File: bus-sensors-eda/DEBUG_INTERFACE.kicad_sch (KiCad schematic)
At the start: 8 parts, among them J2 Generic_Conn_01x05

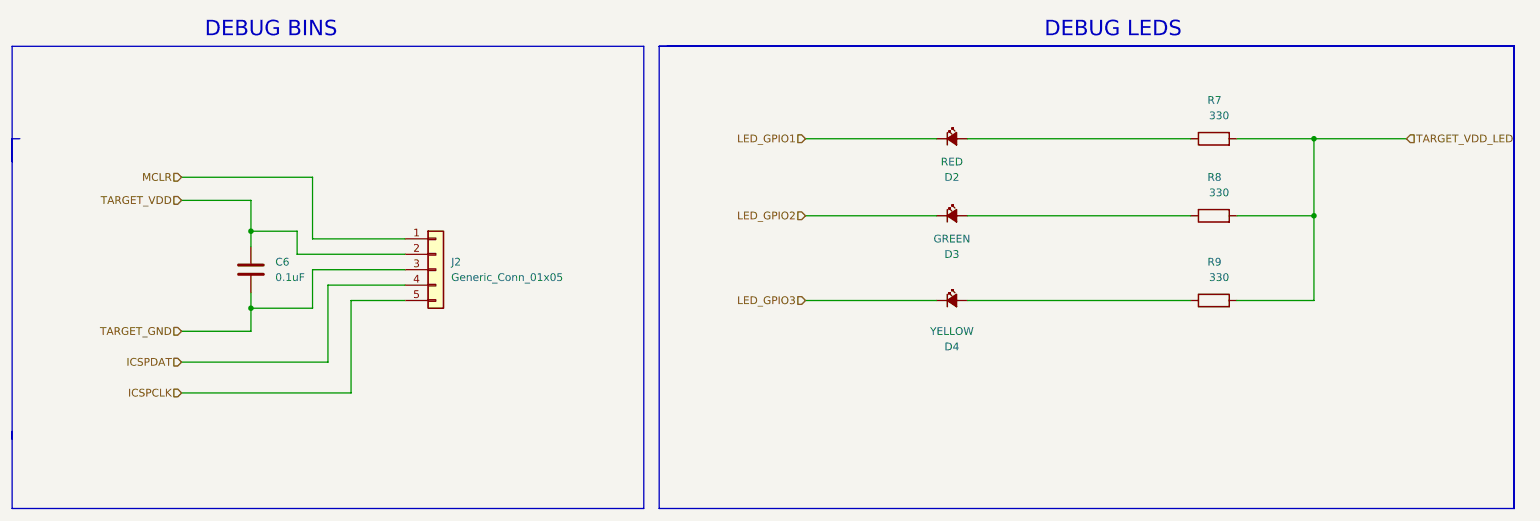
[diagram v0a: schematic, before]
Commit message: moving files under eda dir
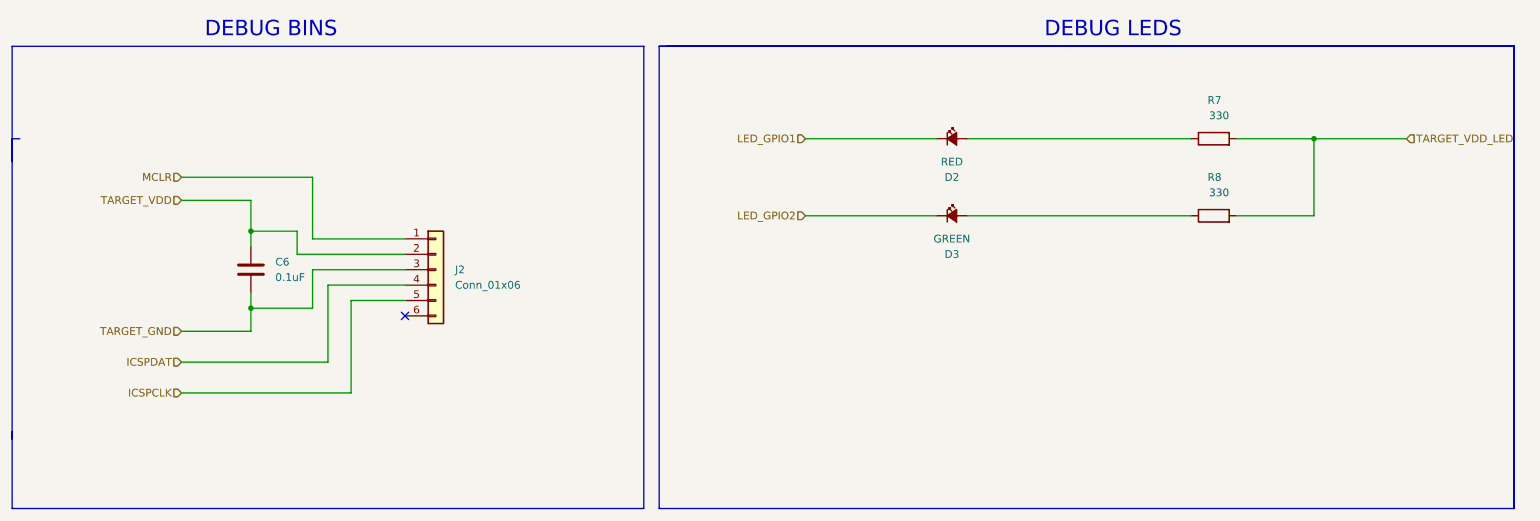
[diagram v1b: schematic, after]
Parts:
- removed D4: YELLOW, LED_SMD:LED_2512_6332Metric_Pad1.52x3.35mm_HandSolder, symbol Device:LED_Small_Filled
- removed J2: Generic_Conn_01x05, Connector_PinHeader_2.54mm:PinHeader_1x05_P2.54mm_Vertical, symbol avionics_board-cache:Connector_Generic_Conn_01x05
- removed R9: 330, Resistor_SMD:R_1210_3225Metric_Pad1.30x2.65mm_HandSolder, symbol Device:R
- added J2: Conn_01x06, Connector_PinHeader_2.54mm:PinHeader_1x06_P2.54mm_Horizontal, symbol Connector_Generic:Conn_01x06
- C6: footprint Capacitor_SMD:C_1812_4532Metric_Pad1.57x3.40mm_HandSolder -> Capacitor_SMD:C_1210_3225Metric_Pad1.33x2.70mm_HandSolder
- D2, D3: footprint LED_SMD:LED_2512_6332Metric_Pad1.52x3.35mm_HandSolder -> LED_SMD:LED_2010_5025Metric_Pad1.52x2.65mm_HandSolder
- R7, R8: footprint Resistor_SMD:R_1210_3225Metric_Pad1.30x2.65mm_HandSolder -> Resistor_SMD:R_2010_5025Metric_Pad1.40x2.65mm_HandSolder
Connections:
- net ICSPCLK: now also J2.5 (Pin_5)
- net ICSPDAT: now also J2.4 (Pin_4)
- net MCLR: now also J2.1 (Pin_1)
- net TARGET_GND: now also J2.3 (Pin_3)
- net TARGET_VDD: now also J2.2 (Pin_2)
- no-connect marks 0 -> 1
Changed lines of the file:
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@@
 (kicad_sch (version 20211123) (generator eeschema)
   (paper "A3")
-  (junction (at 288.29 83.82) (diameter 0) (color 0 0 0 0)
-  )
   (junction (at 288.29 71.12) (diameter 0) (color 0 0 0 0)
   )
@@
   (junction (at 113.03 99.06) (diameter 0) (color 0 0 0 0)
   )
+  (no_connect (at 138.43 100.33))
   (wire (pts (xy 113.03 99.06) (xy 113.03 96.52))
     (stroke (width 0) (type default) (color 0 0 0 0))
@@
     (stroke (width 0) (type default) (color 0 0 0 0))
   )
-  (wire (pts (xy 204.47 97.79) (xy 226.06 97.79))
-    (stroke (width 0) (type default) (color 0 0 0 0))
-  )
   (wire (pts (xy 275.59 83.82) (xy 288.29 83.82))
     (stroke (width 0) (type default) (color 0 0 0 0))
@@
     (stroke (width 0) (type default) (color 0 0 0 0))
   )
-  (wire (pts (xy 288.29 97.79) (xy 288.29 83.82))
-    (stroke (width 0) (type default) (color 0 0 0 0))
-  )
   (polyline (pts (xy 180.34 132.08) (xy 180.34 55.88))
     (stroke (width 0) (type default) (color 0 0 0 0))
@@
     (stroke (width 0) (type default) (color 0 0 0 0))
   )
-  (wire (pts (xy 231.14 97.79) (xy 267.97 97.79))
-    (stroke (width 0) (type default) (color 0 0 0 0))
-  )
   (wire (pts (xy 204.47 83.82) (xy 226.06 83.82))
     (stroke (width 0) (type default) (color 0 0 0 0))
   )
   (polyline (pts (xy 180.34 55.88) (xy 321.31 55.88))
-    (stroke (width 0) (type default) (color 0 0 0 0))
-  )
-  (wire (pts (xy 275.59 97.79) (xy 288.29 97.79))
     (stroke (width 0) (type default) (color 0 0 0 0))
   )
@@
     (effects (font (size 2.54 2.54)) (justify left bottom))
   )
-  (hierarchical_label "LED_GPIO3" (shape input) (at 204.47 97.79 180)
-    (effects (font (size 1.27 1.27)) (justify right))
-  )
   (hierarchical_label "MCLR" (shape input) (at 101.6 77.47 180)
     (effects (font (size 1.27 1.27)) (justify right))
@@
       (effects (font (size 1.27 1.27)) (justify left))
     )
-    (property "Footprint" "Resistor_SMD:R_1210_3225Metric_Pad1.30x2.65mm_HandSolder" (id 2) (at 271.78 72.898 90)
+    (property "Footprint" "Resistor_SMD:R_2010_5025Metric_Pad1.40x2.65mm_HandSolder" (id 2) (at 271.78 72.898 90)
       (effects (font (size 1.27 1.27)) hide)
     )
@@
     (pin "2")
   )
-  (symbol (lib_id "Device:LED_Small_Filled") (at 228.6 97.79 0) (unit 1)
-    (in_bom yes) (on_board yes)
-    (property "Reference" "D4" (id 0) (at 228.6 105.41 0))
-    (property "Value" "YELLOW" (id 1) (at 228.6 102.87 0))
-    (property "Footprint" "LED_SMD:LED_2512_6332Metric_Pad1.52x3.35mm_HandSolder" (id 2) (at 228.6 97.79 90)
-      (effects (font (size 1.27 1.27)) hide)
-    )
-    (property "Datasheet" "~" (id 3) (at 228.6 97.79 90)
-      (effects (font (size 1.27 1.27)) hide)
-    )
-    (pin "1")
-    (pin "2")
-  )
   (symbol (lib_id "Device:C") (at 113.03 92.71 180) (unit 1)
     (in_bom yes) (on_board yes)
@@
       (effects (font (size 1.27 1.27)) (justify left))
     )
-    (property "Footprint" "Capacitor_SMD:C_1812_4532Metric_Pad1.57x3.40mm_HandSolder" (id 2) (at 112.0648 88.9 0)
+    (property "Footprint" "Capacitor_SMD:C_1210_3225Metric_Pad1.33x2.70mm_HandSolder" (id 2) (at 112.0648 88.9 0)
       (effects (font (size 1.27 1.27)) hide)
     )
@@
     (property "Reference" "D2" (id 0) (at 228.6 77.47 0))
     (property "Value" "RED" (id 1) (at 228.6 74.93 0))
-    (property "Footprint" "LED_SMD:LED_2512_6332Metric_Pad1.52x3.35mm_HandSolder" (id 2) (at 228.6 71.12 90)
+    (property "Footprint" "LED_SMD:LED_2010_5025Metric_Pad1.52x2.65mm_HandSolder" (id 2) (at 228.6 71.12 90)
       (effects (font (size 1.27 1.27)) hide)
     )
@@
     (pin "2")
   )
-  (symbol (lib_id "Device:R") (at 271.78 97.79 90) (unit 1)
-    (in_bom yes) (on_board yes)
-    (property "Reference" "R9" (id 0) (at 273.05 91.44 90)
-      (effects (font (size 1.27 1.27)) (justify left))
-    )
-    (property "Value" "330" (id 1) (at 274.32 93.98 90)
-      (effects (font (size 1.27 1.27)) (justify left))
-    )
-    (property "Footprint" "Resistor_SMD:R_1210_3225Metric_Pad1.30x2.65mm_HandSolder" (id 2) (at 271.78 99.568 90)
-      (effects (font (size 1.27 1.27)) hide)
-    )
-    (property "Datasheet" "~" (id 3) (at 271.78 97.79 0)
-      (effects (font (size 1.27 1.27)) hide)
-    )
-    (pin "1")
-    (pin "2")
-  )
-  (symbol (lib_id "avionics_board-cache:Connector_Generic_Conn_01x05") (at 143.51 92.71 0) (unit 1)
+  (symbol (lib_id "Connector_Generic:Conn_01x06") (at 143.51 92.71 0) (unit 1)
     (in_bom yes) (on_board yes) (fields_autoplaced)
-    (property "Reference" "J2" (id 0) (at 146.05 91.4399 0)
-      (effects (font (size 1.27 1.27)) (justify left))
-    )
-    (property "Value" "Generic_Conn_01x05" (id 1) (at 146.05 93.9799 0)
-      (effects (font (size 1.27 1.27)) (justify left))
-    )
-    (property "Footprint" "Connector_PinHeader_2.54mm:PinHeader_1x05_P2.54mm_Vertical" (id 2) (at 143.51 92.71 0)
-      (effects (font (size 1.27 1.27)) hide)
-    )
-    (property "Datasheet" "" (id 3) (at 143.51 92.71 0)
+    (property "Reference" "J2" (id 0) (at 146.685 92.7099 0)
+      (effects (font (size 1.27 1.27)) (justify left))
+    )
+    (property "Value" "Conn_01x06" (id 1) (at 146.685 95.2499 0)
+      (effects (font (size 1.27 1.27)) (justify left))
+    )
+    (property "Footprint" "Connector_PinHeader_2.54mm:PinHeader_1x06_P2.54mm_Horizontal" (id 2) (at 143.51 92.71 0)
+      (effects (font (size 1.27 1.27)) hide)
+    )
+    (property "Datasheet" "~" (id 3) (at 143.51 92.71 0)
       (effects (font (size 1.27 1.27)) hide)
     )
@@
     (pin "4")
     (pin "5")
+    (pin "6")
   )
   (symbol (lib_id "Device:LED_Small_Filled") (at 228.6 83.82 0) (unit 1)
@@
     (property "Reference" "D3" (id 0) (at 228.6 90.17 0))
     (property "Value" "GREEN" (id 1) (at 228.6 87.63 0))
-    (property "Footprint" "LED_SMD:LED_2512_6332Metric_Pad1.52x3.35mm_HandSolder" (id 2) (at 228.6 83.82 90)
+    (property "Footprint" "LED_SMD:LED_2010_5025Metric_Pad1.52x2.65mm_HandSolder" (id 2) (at 228.6 83.82 90)
       (effects (font (size 1.27 1.27)) hide)
     )
@@
       (effects (font (size 1.27 1.27)) (justify left))
     )
-    (property "Footprint" "Resistor_SMD:R_1210_3225Metric_Pad1.30x2.65mm_HandSolder" (id 2) (at 271.78 85.598 90)
-      (effects (font (size 1.27 1.27)) hide)
-    )
+    (property "Footprint" "Resistor_SMD:R_2010_5025Metric_Pad1.40x2.65mm_HandSolder" (id 2) (at 271.78 85.598 90)
+      (effects (font (size 1.27 1.27)) hide)
+    )
